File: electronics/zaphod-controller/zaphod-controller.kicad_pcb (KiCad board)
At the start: 4 copper layers, 199.9 x 69.3 mm, 247 parts, among them P1 MOLEX_43160-0102, P11 MOLEX_MINIFIT_JR_2x4_WAY, P12 MOLEX_MINIFIT_JR_2x4_WAY, P13 MOLEX_MINIFIT_JR_2x4_WAY, P14 MOLEX_MINIFIT_JR_2x4_WAY, P15 MOLEX_NANOFIT_2x4_WAY, P16 MOLEX_NANOFIT_1x6_WAY, P17 MOLEX_NANOFIT_2x3_WAY, P18 CONN_01X02, P19 MOLEX_KK2.54_1x4_WAY_FAN, P2 MOLEX_MINIFIT_JR_2x2_WAY, P20 CONN_01X06, P21 MOLEX_NANOFIT_2x5_WAY, P3 MOLEX_MINIFIT_JR_2x2_WAY, P4 MOLEX_MINIFIT_JR_2x2_WAY, P5 MOLEX_MINIFIT_JR_2x2_WAY, Q1 Si7852DP, Q2 Si7852DP, Q3 2N7002P, Q4 NTR1P02T1G, Q5 BC847B, Q6 2N7002P, SW1 B3U-1000P_SPST-NO_SMD, SW2 B3U-1000P_SPST-NO_SMD, SW3 B3U-1000P_SPST-NO_SMD, U1 ISL85410FRZ, U10 ULN2003A, U11 ULN2003A, U12 ADUM5412, U2 LM5116, U3 ISL85410FRZ, U4 STM32F429VET6, U5 ADUM3160, U6 ACS711KEXLT_15AB, U7 ACS711KEXLT_15AB, U8 ACS711KEXLT_15AB, U9 ACS711KEXLT_15AB, X1 CSTCE8M00G55Z, X2 SWD_SMT_SOCKET, X3 ABS06-107-32.768KHZ

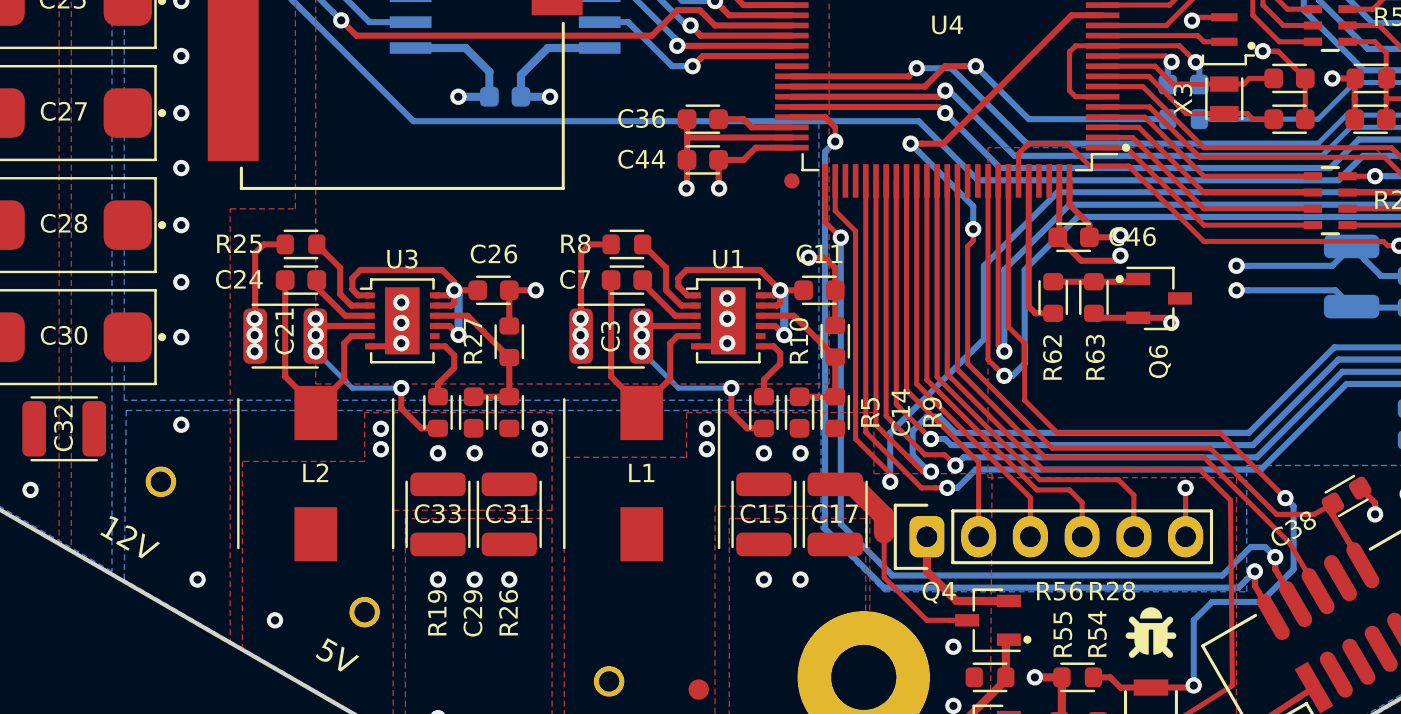
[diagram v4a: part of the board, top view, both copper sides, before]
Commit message: Added buzzer, notes on pcb sheets
Dimensions, stack info, etc.
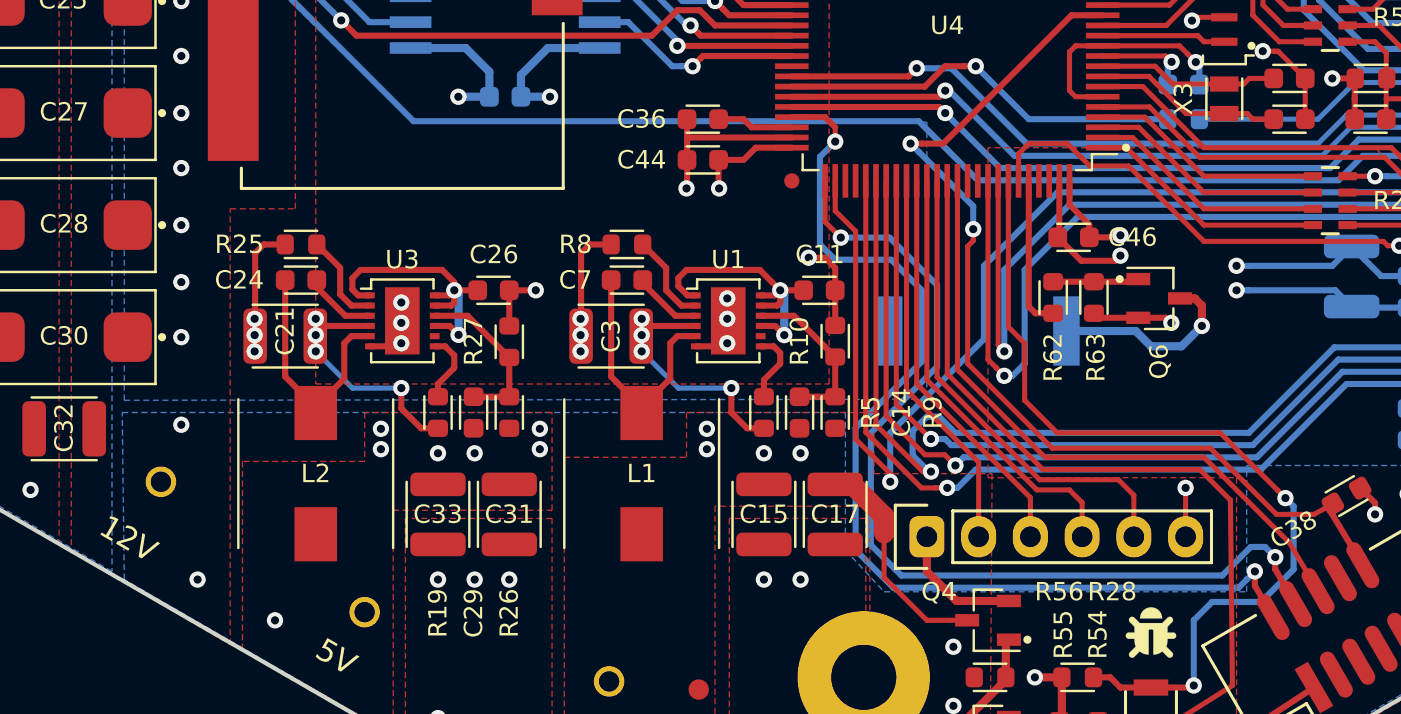
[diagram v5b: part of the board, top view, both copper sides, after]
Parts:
- added LS1: PKMCS0909E4000-R1, Applidyne_Special:MURATA_PKMCS0909E4000, B.Cu at (163.5, 97.0)
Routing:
- net Net-(LS1-Pad2): track 0.00 -> 9.59 mm, vias 0 -> 1
- net SWDIO: track 47.4 -> 51.6 mm
- net SWCLK: track 42.9 -> 46.7 mm
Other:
- board text added: "White Soldermask Black Silkscreen ENIG Surface Finish 1.6mm or 2.0mm FR4 4 layers - 2oz (70um) copper 200x70 mm ext dimensions"

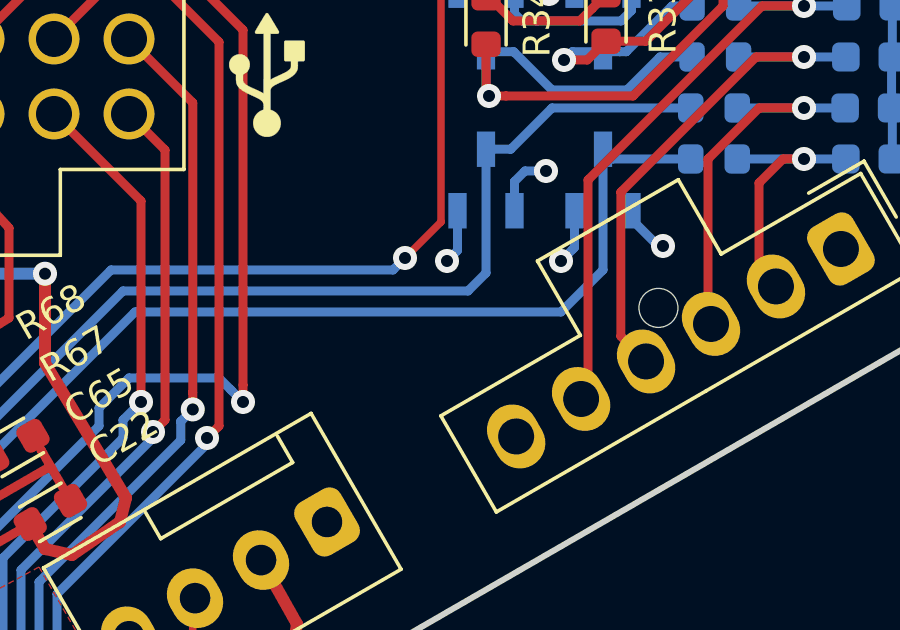
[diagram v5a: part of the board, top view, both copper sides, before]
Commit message: Added additional silkscreen labels
Added UART pinout on bottom, symbol on uart/i2c expansion connector
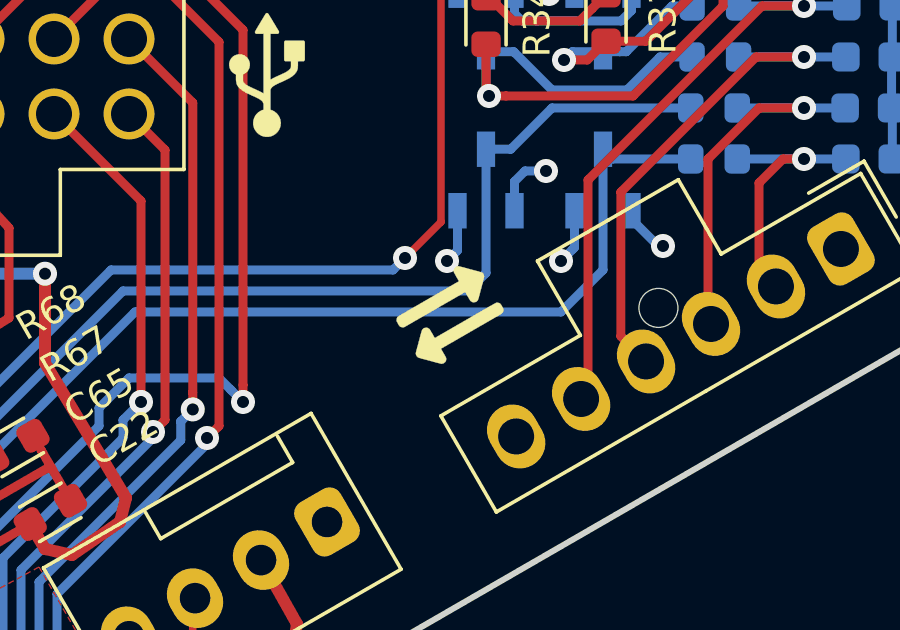
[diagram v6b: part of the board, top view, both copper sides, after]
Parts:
- added LOGO13: LOGO, Applidyne_Logo:DUPLEX_LOGO330X260, F.Cu at (223.9, 82.3)
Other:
- board text added: "3V"
- board text added: "CTS"
- board text added: "RTS"
- board text added: "RX"
- board text added: "TX"
